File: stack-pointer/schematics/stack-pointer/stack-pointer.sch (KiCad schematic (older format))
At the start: 15 parts

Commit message: added index register
Also fixed hardware design bugs and updated readme.
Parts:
- added U?: 74LS04, symbol 74xx:74LS04
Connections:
- net SUB: now also U?.5; no longer U?.1 (U/~D), U?.1 (U/~D), U?.1 (U/~D), U?.1 (U/~D)
- new net: U?.1 (U/~D), U?.1 (U/~D), U?.1 (U/~D), U?.1 (U/~D), U?.6
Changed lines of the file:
@@
 Wire Wire Line
 	2075 2025 3975 2025
-Text HLabel 10450 1900 2    50   Input ~ 0
+Text HLabel 10450 2150 2    50   Input ~ 0
 CLK
 Wire Wire Line
 	8000 2250 8000 1800
 Wire Wire Line
-	8000 1800 10450 1800
+	8000 1800 9675 1800
 Wire Wire Line
 	5775 2250 5775 1800
@@
 Wire Wire Line
 	7500 2250 7500 1900
-Connection ~ 7500 1900
-Wire Wire Line
-	7500 1900 10450 1900
 $Comp
 L 74xx:74LS32 U?
@@
 $EndComp
 NoConn ~ 1475 3250
+$Comp
+L 74xx:74LS04 U?
+U 3 1 6192DA09
+P 9975 1800
+F 0 "U?" H 10050 1925 50  0000 C CNN
+F 1 "74LS04" H 10100 1675 50  0000 C CNN
+F 2 "" H 9975 1800 50  0001 C CNN
+F 3 "http://www.ti.com/lit/gpn/sn74LS04" H 9975 1800 50  0001 C CNN
+	3    9975 1800
+	-1   0    0    1
+$EndComp
+Wire Wire Line
+	10275 1800 10450 1800
+Wire Wire Line
+	7500 1900 9150 1900
+Wire Wire Line
+	9150 1900 9150 2150
+Wire Wire Line
+	9150 2150 10450 2150
+Connection ~ 7500 1900
 $EndSCHEMATC

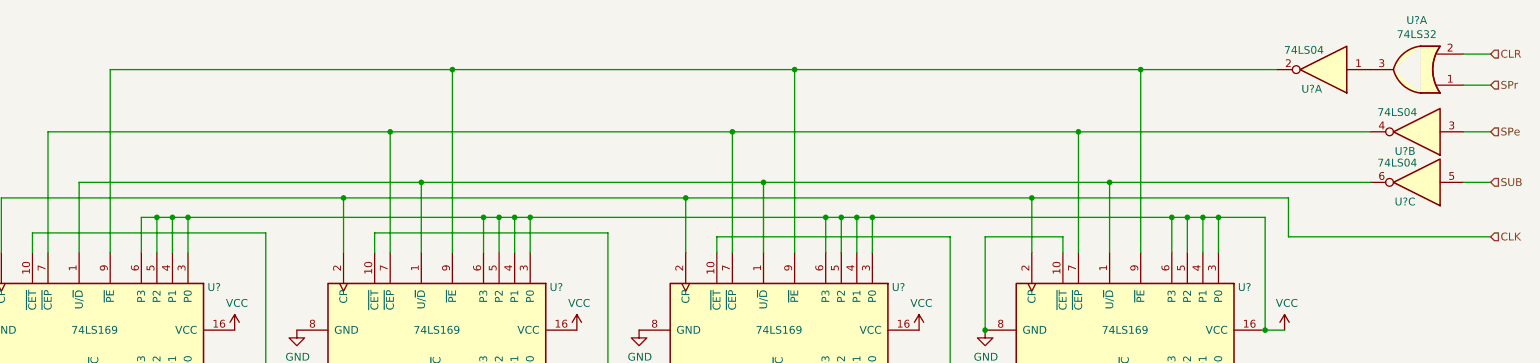
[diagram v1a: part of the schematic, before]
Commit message: removed ineffectual CLR line to stack pointer
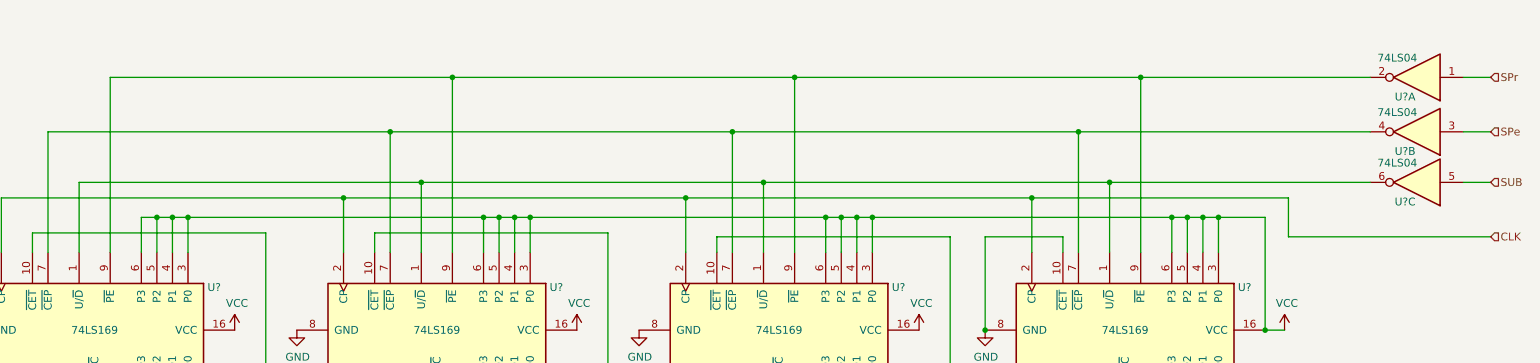
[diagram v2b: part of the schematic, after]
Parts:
- removed U?: 74LS32, symbol 74xx:74LS32
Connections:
- net SPr: now also U?.1
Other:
- moved on the sheet: U?A
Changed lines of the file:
@@
 	7500 2250 7500 1900
-$Comp
-L 74xx:74LS32 U?
-U 1 1 61733C03
-P 9975 1075
-F 0 "U?" H 9975 758 50  0000 C CNN
-F 1 "74LS32" H 9975 849 50  0000 C CNN
-F 2 "" H 9975 1075 50  0001 C CNN
-F 3 "http://www.ti.com/lit/gpn/sn74LS32" H 9975 1075 50  0001 C CNN
-	1    9975 1075
-	-1   0    0    1
-$EndComp
 $Comp
 L 74xx:74LS04 U?
 U 1 1 617377D7
-P 9375 1075
-F 0 "U?" H 9450 1200 50  0000 C CNN
-F 1 "74LS04" H 9500 950 50  0000 C CNN
-F 2 "" H 9375 1075 50  0001 C CNN
-F 3 "http://www.ti.com/lit/gpn/sn74LS04" H 9375 1075 50  0001 C CNN
-	1    9375 1075
+P 9975 1125
+F 0 "U?" H 10050 1250 50  0000 C CNN
+F 1 "74LS04" H 10100 1000 50  0000 C CNN
+F 2 "" H 9975 1125 50  0001 C CNN
+F 3 "http://www.ti.com/lit/gpn/sn74LS04" H 9975 1125 50  0001 C CNN
+	1    9975 1125
 	-1   0    0    1
 $EndComp
@@
 	9675 1475 7800 1475
 Connection ~ 7800 1475
-Text HLabel 10450 1175 2    50   Input ~ 0
+Text HLabel 10450 1125 2    50   Input ~ 0
 SPr
-Text HLabel 10450 975  2    50   Input ~ 0
-CLR
-Wire Wire Line
-	10450 975  10275 975
-Wire Wire Line
-	10450 1175 10275 1175
-Wire Wire Line
-	8200 1075 8200 2250
-Wire Wire Line
-	8200 1075 5975 1075
-Wire Wire Line
-	5975 1075 5975 2250
-Connection ~ 8200 1075
-Wire Wire Line
-	8200 1075 9075 1075
-Wire Wire Line
-	5975 1075 3775 1075
-Wire Wire Line
-	3775 1075 3775 2250
-Connection ~ 5975 1075
-Wire Wire Line
-	3775 1075 1575 1075
-Wire Wire Line
-	1575 1075 1575 2250
-Connection ~ 3775 1075
+Wire Wire Line
+	8200 1125 8200 2250
+Wire Wire Line
+	8200 1125 5975 1125
+Wire Wire Line
+	5975 1125 5975 2250
+Connection ~ 8200 1125
+Wire Wire Line
+	8200 1125 9675 1125
+Wire Wire Line
+	5975 1125 3775 1125
+Wire Wire Line
+	3775 1125 3775 2250
+Connection ~ 5975 1125
+Wire Wire Line
+	3775 1125 1575 1125
+Wire Wire Line
+	1575 1125 1575 2250
+Connection ~ 3775 1125
 $Comp
 L 74xx:74LS245 U?
@@
 	9150 2150 10450 2150
 Connection ~ 7500 1900
+Wire Wire Line
+	10450 1125 10275 1125
 $EndSCHEMATC

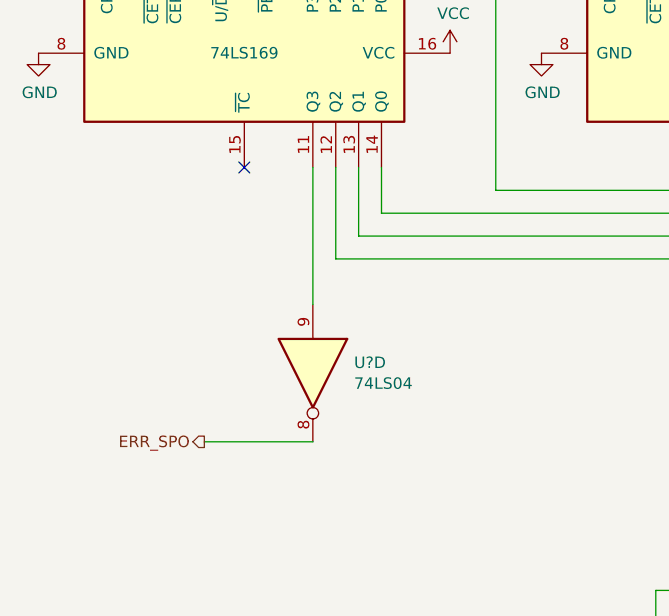
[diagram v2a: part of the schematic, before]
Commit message: removed stack pointer and index register error flags
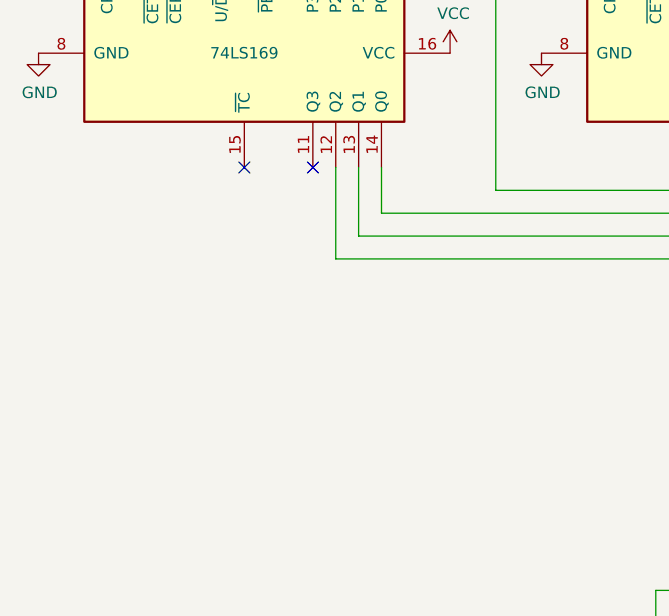
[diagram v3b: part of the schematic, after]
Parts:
- removed U?: 74LS04, symbol 74xx:74LS04
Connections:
- no-connect marks 1 -> 2
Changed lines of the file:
@@
 Wire Wire Line
 	6875 6350 6875 6625
-$Comp
-L 74xx:74LS04 U?
-U 4 1 6184D6B7
-P 1775 4150
-F 0 "U?" V 1729 4330 50  0000 L CNN
-F 1 "74LS04" V 1820 4330 50  0000 L CNN
-F 2 "" H 1775 4150 50  0001 C CNN
-F 3 "http://www.ti.com/lit/gpn/sn74LS04" H 1775 4150 50  0001 C CNN
-	4    1775 4150
-	0    1    1    0
-$EndComp
-Text HLabel 1300 4450 0    50   Output ~ 0
-ERR_SPO
-Wire Wire Line
-	1300 4450 1775 4450
-Wire Wire Line
-	1775 3850 1775 3250
 Wire Wire Line
 	10275 5100 10325 5100
@@
 Wire Wire Line
 	10450 1125 10275 1125
+NoConn ~ 1775 3250
 $EndSCHEMATC

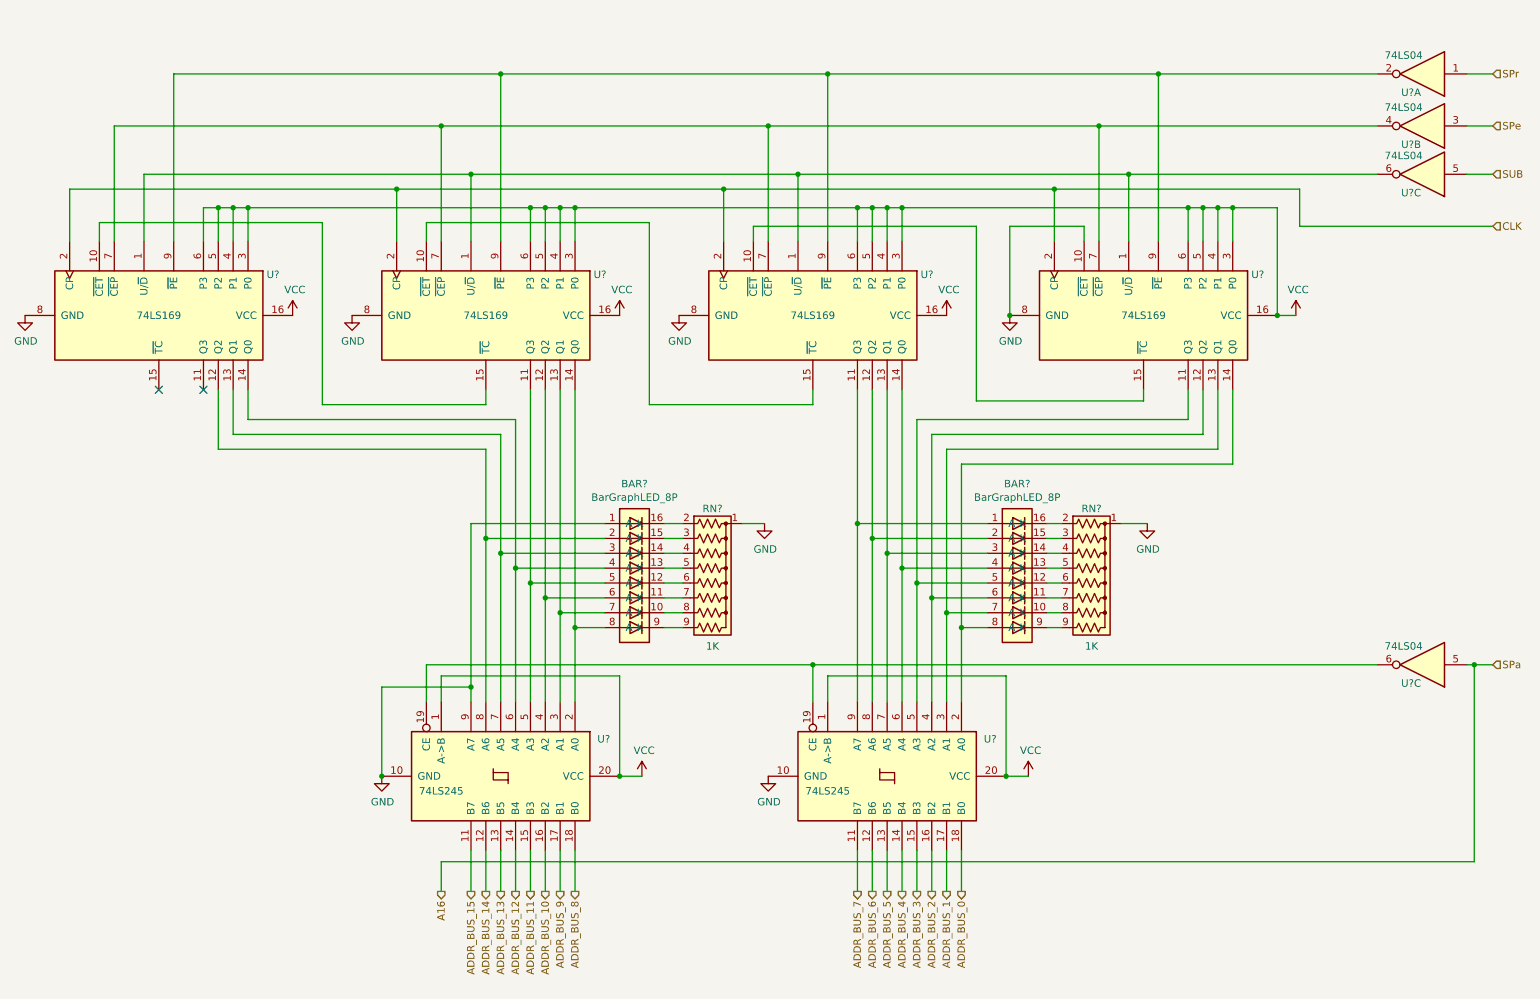
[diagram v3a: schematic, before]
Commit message: added schematics to documentation
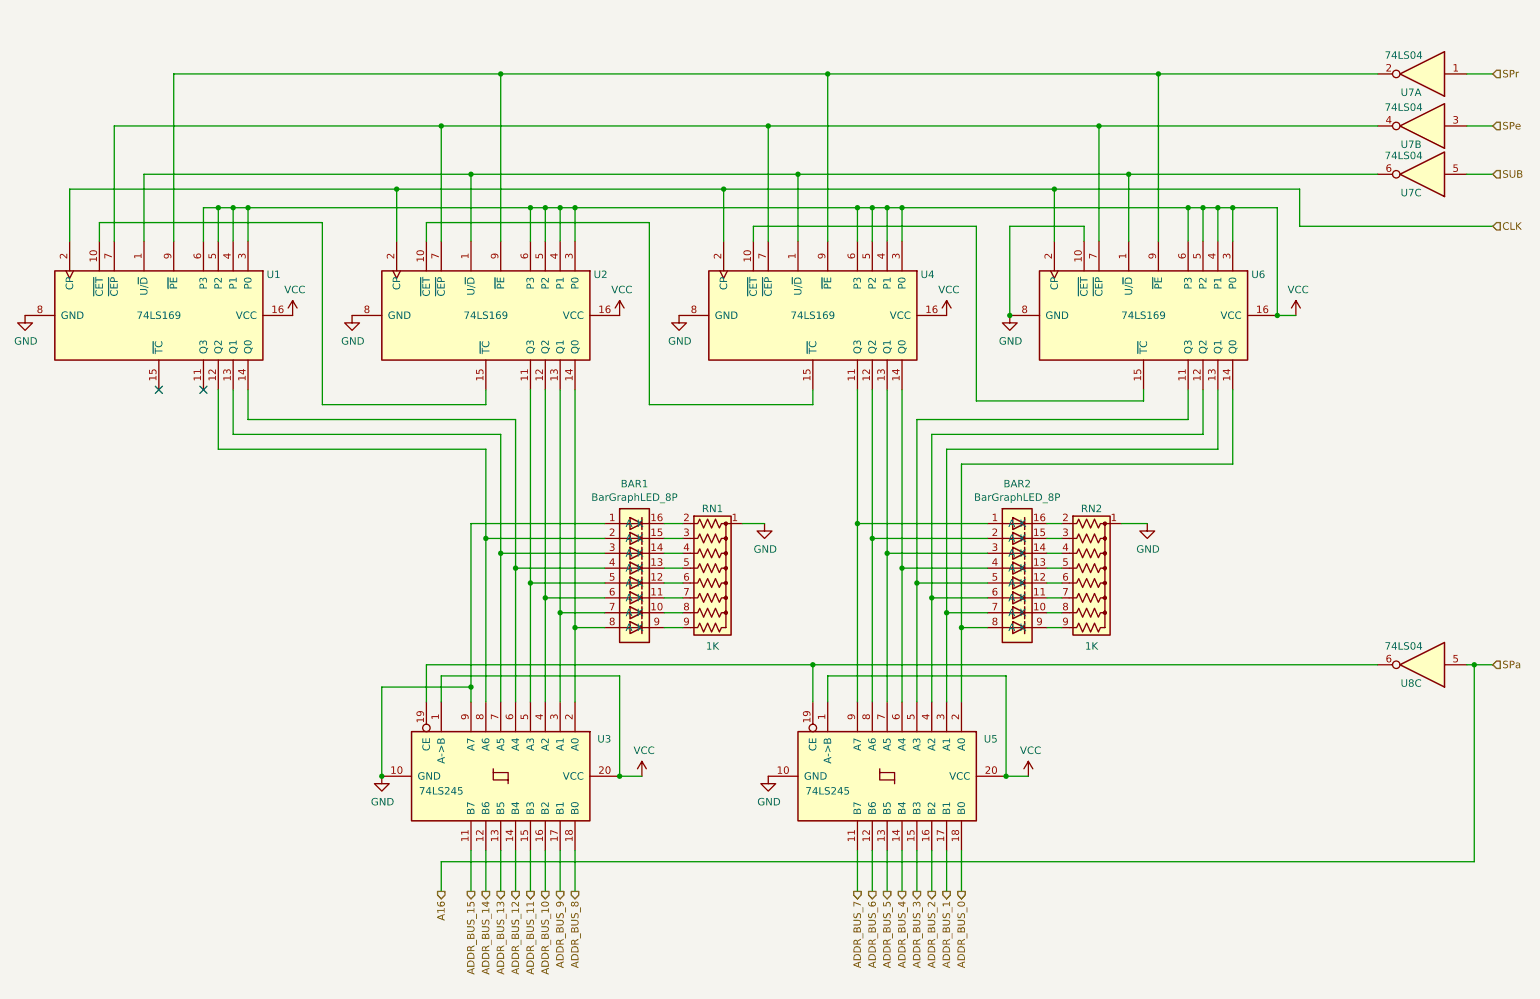
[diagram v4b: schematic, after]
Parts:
- gave numbers to parts that had none: 12
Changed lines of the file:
@@
 Rev ""
 Comp ""
-Comment1 ""
-Comment2 ""
-Comment3 ""
+Comment1 "SPr - Reset stack pointer registers to empty stack value"
+Comment2 "SPe - increment or decrement value according to SUB"
+Comment3 "SPa - write stack pointer value to address bus and activate A16"
 Comment4 ""
 $EndDescr
 $Comp
-L 74xx:74LS169 U?
+L 74xx:74LS169 U6
 U 1 1 6170A50B
 P 8100 2750
-F 0 "U?" V 7825 3475 50  0000 L CNN
+F 0 "U6" V 7825 3475 50  0000 L CNN
 F 1 "74LS169" V 8100 2600 50  0000 L CNN
 F 2 "" H 8100 2750 50  0001 C CNN
@@
 $EndComp
 $Comp
-L 74xx:74LS169 U?
+L 74xx:74LS169 U4
 U 1 1 6170CC22
 P 5875 2750
-F 0 "U?" V 5600 3475 50  0000 L CNN
+F 0 "U4" V 5600 3475 50  0000 L CNN
 F 1 "74LS169" V 5875 2600 50  0000 L CNN
 F 2 "" H 5875 2750 50  0001 C CNN
@@
 $EndComp
 $Comp
-L 74xx:74LS169 U?
+L 74xx:74LS169 U2
 U 1 1 6170EF25
 P 3675 2750
-F 0 "U?" V 3400 3475 50  0000 L CNN
+F 0 "U2" V 3400 3475 50  0000 L CNN
 F 1 "74LS169" V 3675 2600 50  0000 L CNN
 F 2 "" H 3675 2750 50  0001 C CNN
@@
 $EndComp
 $Comp
-L 74xx:74LS169 U?
+L 74xx:74LS169 U1
 U 1 1 61710E64
 P 1475 2750
-F 0 "U?" V 1200 3475 50  0000 L CNN
+F 0 "U1" V 1200 3475 50  0000 L CNN
 F 1 "74LS169" V 1475 2600 50  0000 L CNN
 F 2 "" H 1475 2750 50  0001 C CNN
@@
 	7200 2150 7200 2750
 $Comp
-L power:GND #PWR?
+L power:GND #PWR011
 U 1 1 61723800
 P 7200 2750
-F 0 "#PWR?" H 7200 2500 50  0001 C CNN
+F 0 "#PWR011" H 7200 2500 50  0001 C CNN
 F 1 "GND" H 7205 2577 50  0000 C CNN
 F 2 "" H 7200 2750 50  0001 C CNN
@@
 Connection ~ 8700 2025
 $Comp
-L power:VCC #PWR?
+L power:VCC #PWR014
 U 1 1 6172B5F2
 P 9125 2750
-F 0 "#PWR?" H 9125 2600 50  0001 C CNN
+F 0 "#PWR014" H 9125 2600 50  0001 C CNN
 F 1 "VCC" H 9140 2923 50  0000 C CNN
 F 2 "" H 9125 2750 50  0001 C CNN
@@
 	7500 2250 7500 1900
 $Comp
-L 74xx:74LS04 U?
+L 74xx:74LS04 U7
 U 1 1 617377D7
 P 9975 1125
-F 0 "U?" H 10050 1250 50  0000 C CNN
+F 0 "U7" H 10050 1250 50  0000 C CNN
 F 1 "74LS04" H 10100 1000 50  0000 C CNN
 F 2 "" H 9975 1125 50  0001 C CNN
@@
 $EndComp
 $Comp
-L 74xx:74LS04 U?
+L 74xx:74LS04 U7
 U 2 1 617403AA
 P 9975 1475
-F 0 "U?" H 10050 1600 50  0000 C CNN
+F 0 "U7" H 10050 1600 50  0000 C CNN
 F 1 "74LS04" H 10100 1350 50  0000 C CNN
 F 2 "" H 9975 1475 50  0001 C CNN
@@
 Connection ~ 3775 1125
 $Comp
-L 74xx:74LS245 U?
+L 74xx:74LS245 U5
 U 1 1 61761DC7
 P 6375 5850
-F 0 "U?" V 6125 6500 50  0000 L CNN
+F 0 "U5" V 6125 6500 50  0000 L CNN
 F 1 "74LS245" V 6475 5300 50  0000 L CNN
 F 2 "" H 6375 5850 50  0001 C CNN
@@
 $EndComp
 $Comp
-L 74xx:74LS245 U?
+L 74xx:74LS245 U3
 U 1 1 617651A0
 P 3775 5850
-F 0 "U?" V 3525 6500 50  0000 L CNN
+F 0 "U3" V 3525 6500 50  0000 L CNN
 F 1 "74LS245" V 3875 5300 50  0000 L CNN
 F 2 "" H 3775 5850 50  0001 C CNN
@@
 SPa
 $Comp
-L 74xx:74LS04 U?
+L 74xx:74LS04 U8
 U 3 1 617C6293
 P 9975 5100
-F 0 "U?" H 10050 5225 50  0000 C CNN
+F 0 "U8" H 10050 5225 50  0000 C CNN
 F 1 "74LS04" H 10100 4975 50  0000 C CNN
 F 2 "" H 9975 5100 50  0001 C CNN
@@
 	10325 5100 10450 5100
 $Comp
-L common-symbols:BarGraphLED_8P BAR?
+L common-symbols:BarGraphLED_8P BAR2
 U 1 1 61871F0D
 P 7250 4550
-F 0 "BAR?" H 7250 5217 50  0000 C CNN
+F 0 "BAR2" H 7250 5217 50  0000 C CNN
 F 1 "BarGraphLED_8P" H 7250 5126 50  0000 C CNN
 F 2 "" H 7250 4550 50  0001 C CNN
@@
 $EndComp
 $Comp
-L common-symbols:BarGraphLED_8P BAR?
+L common-symbols:BarGraphLED_8P BAR1
 U 1 1 618760B7
 P 4675 4550
-F 0 "BAR?" H 4675 5217 50  0000 C CNN
+F 0 "BAR1" H 4675 5217 50  0000 C CNN
 F 1 "BarGraphLED_8P" H 4675 5126 50  0000 C CNN
 F 2 "" H 4675 4550 50  0001 C CNN
@@
 	7450 4150 7550 4150
 $Comp
-L power:GND #PWR?
+L power:GND #PWR013
 U 1 1 6190312A
 P 8125 4150
-F 0 "#PWR?" H 8125 3900 50  0001 C CNN
+F 0 "#PWR013" H 8125 3900 50  0001 C CNN
 F 1 "GND" H 8130 3977 50  0000 C CNN
 F 2 "" H 8125 4150 50  0001 C CNN
@@
 	7950 4150 8125 4150
 $Comp
-L Device:R_Network08_US RN?
+L Device:R_Network08_US RN2
 U 1 1 6187D438
 P 7750 4550
-F 0 "RN?" V 7250 4550 50  0000 C CNN
+F 0 "RN2" V 7250 4550 50  0000 C CNN
 F 1 "1K" V 8175 4550 50  0000 C CNN
 F 2 "Resistor_THT:R_Array_SIP9" V 8225 4550 50  0001 C CNN
@@
 $EndComp
 $Comp
-L Device:R_Network08_US RN?
+L Device:R_Network08_US RN1
 U 1 1 6190C19A
 P 5200 4550
-F 0 "RN?" V 4700 4550 50  0000 C CNN
+F 0 "RN1" V 4700 4550 50  0000 C CNN
 F 1 "1K" V 5625 4550 50  0000 C CNN
 F 2 "Resistor_THT:R_Array_SIP9" V 5675 4550 50  0001 C CNN
@@
 	4875 4850 5000 4850
 $Comp
-L power:GND #PWR?
+L power:GND #PWR08
 U 1 1 619B2D32
 P 5550 4150
-F 0 "#PWR?" H 5550 3900 50  0001 C CNN
+F 0 "#PWR08" H 5550 3900 50  0001 C CNN
 F 1 "GND" H 5555 3977 50  0000 C CNN
 F 2 "" H 5550 4150 50  0001 C CNN
@@
 	5550 4150 5400 4150
 $Comp
-L power:GND #PWR?
+L power:GND #PWR04
 U 1 1 619BE970
 P 2975 5850
-F 0 "#PWR?" H 2975 5600 50  0001 C CNN
+F 0 "#PWR04" H 2975 5600 50  0001 C CNN
 F 1 "GND" H 2980 5677 50  0000 C CNN
 F 2 "" H 2975 5850 50  0001 C CNN
@@
 Connection ~ 2975 5850
 $Comp
-L power:GND #PWR?
+L power:GND #PWR09
 U 1 1 619BEE31
 P 5575 5850
-F 0 "#PWR?" H 5575 5600 50  0001 C CNN
+F 0 "#PWR09" H 5575 5600 50  0001 C CNN
 F 1 "GND" H 5580 5677 50  0000 C CNN
 F 2 "" H 5575 5850 50  0001 C CNN
@@
 $EndComp
 $Comp
-L power:VCC #PWR?
+L power:VCC #PWR012
 U 1 1 619BF9DF
 P 7325 5850
-F 0 "#PWR?" H 7325 5700 50  0001 C CNN
+F 0 "#PWR012" H 7325 5700 50  0001 C CNN
 F 1 "VCC" H 7340 6023 50  0000 C CNN
 F 2 "" H 7325 5850 50  0001 C CNN
@@
 Connection ~ 7175 5850
 $Comp
-L power:VCC #PWR?
+L power:VCC #PWR06
 U 1 1 619CBC9F
 P 4725 5850
-F 0 "#PWR?" H 4725 5700 50  0001 C CNN
+F 0 "#PWR06" H 4725 5700 50  0001 C CNN
 F 1 "VCC" H 4740 6023 50  0000 C CNN
 F 2 "" H 4725 5850 50  0001 C CNN
@@
 Connection ~ 4575 5850
 $Comp
-L power:VCC #PWR?
+L power:VCC #PWR010
 U 1 1 619D8E63
 P 6775 2750
-F 0 "#PWR?" H 6775 2600 50  0001 C CNN
+F 0 "#PWR010" H 6775 2600 50  0001 C CNN
 F 1 "VCC" H 6790 2923 50  0000 C CNN
 F 2 "" H 6775 2750 50  0001 C CNN
@@
 $EndComp
 $Comp
-L power:VCC #PWR?
+L power:VCC #PWR05
 U 1 1 619D944E
 P 4575 2750
-F 0 "#PWR?" H 4575 2600 50  0001 C CNN
+F 0 "#PWR05" H 4575 2600 50  0001 C CNN
 F 1 "VCC" H 4590 2923 50  0000 C CNN
 F 2 "" H 4575 2750 50  0001 C CNN
@@
 $EndComp
 $Comp
-L power:VCC #PWR?
+L power:VCC #PWR02
 U 1 1 619D9A49
 P 2375 2750
-F 0 "#PWR?" H 2375 2600 50  0001 C CNN
+F 0 "#PWR02" H 2375 2600 50  0001 C CNN
 F 1 "VCC" H 2390 2923 50  0000 C CNN
 F 2 "" H 2375 2750 50  0001 C CNN
@@
 $EndComp
 $Comp
-L power:GND #PWR?
+L power:GND #PWR01
 U 1 1 619DA07F
 P 575 2750
-F 0 "#PWR?" H 575 2500 50  0001 C CNN
+F 0 "#PWR01" H 575 2500 50  0001 C CNN
 F 1 "GND" H 580 2577 50  0000 C CNN
 F 2 "" H 575 2750 50  0001 C CNN
@@
 $EndComp
 $Comp
-L power:GND #PWR?
+L power:GND #PWR03
 U 1 1 619DA682
 P 2775 2750
-F 0 "#PWR?" H 2775 2500 50  0001 C CNN
+F 0 "#PWR03" H 2775 2500 50  0001 C CNN
 F 1 "GND" H 2780 2577 50  0000 C CNN
 F 2 "" H 2775 2750 50  0001 C CNN
@@
 $EndComp
 $Comp
-L power:GND #PWR?
+L power:GND #PWR07
 U 1 1 619DAC91
 P 4975 2750
-F 0 "#PWR?" H 4975 2500 50  0001 C CNN
+F 0 "#PWR07" H 4975 2500 50  0001 C CNN
 F 1 "GND" H 4980 2577 50  0000 C CNN
 F 2 "" H 4975 2750 50  0001 C CNN
@@
 NoConn ~ 1475 3250
 $Comp
-L 74xx:74LS04 U?
+L 74xx:74LS04 U7
 U 3 1 6192DA09
 P 9975 1800
-F 0 "U?" H 10050 1925 50  0000 C CNN
+F 0 "U7" H 10050 1925 50  0000 C CNN
 F 1 "74LS04" H 10100 1675 50  0000 C CNN
 F 2 "" H 9975 1800 50  0001 C CNN
